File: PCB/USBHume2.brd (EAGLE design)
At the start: 45.1 x 29.8 mm, 23 parts, among them IC1 LM1117MP-3.3

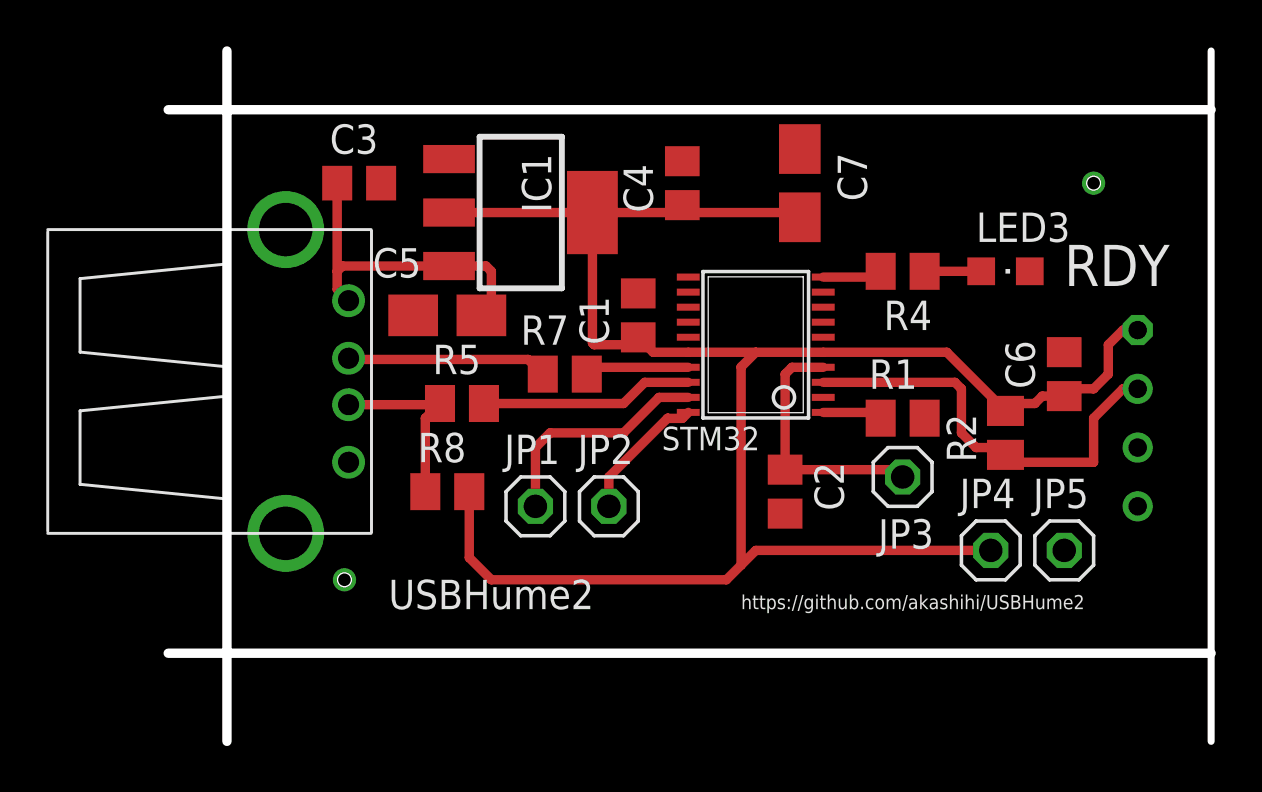
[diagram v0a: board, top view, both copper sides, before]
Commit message: Parts sizes fixed. Board errors fixed.
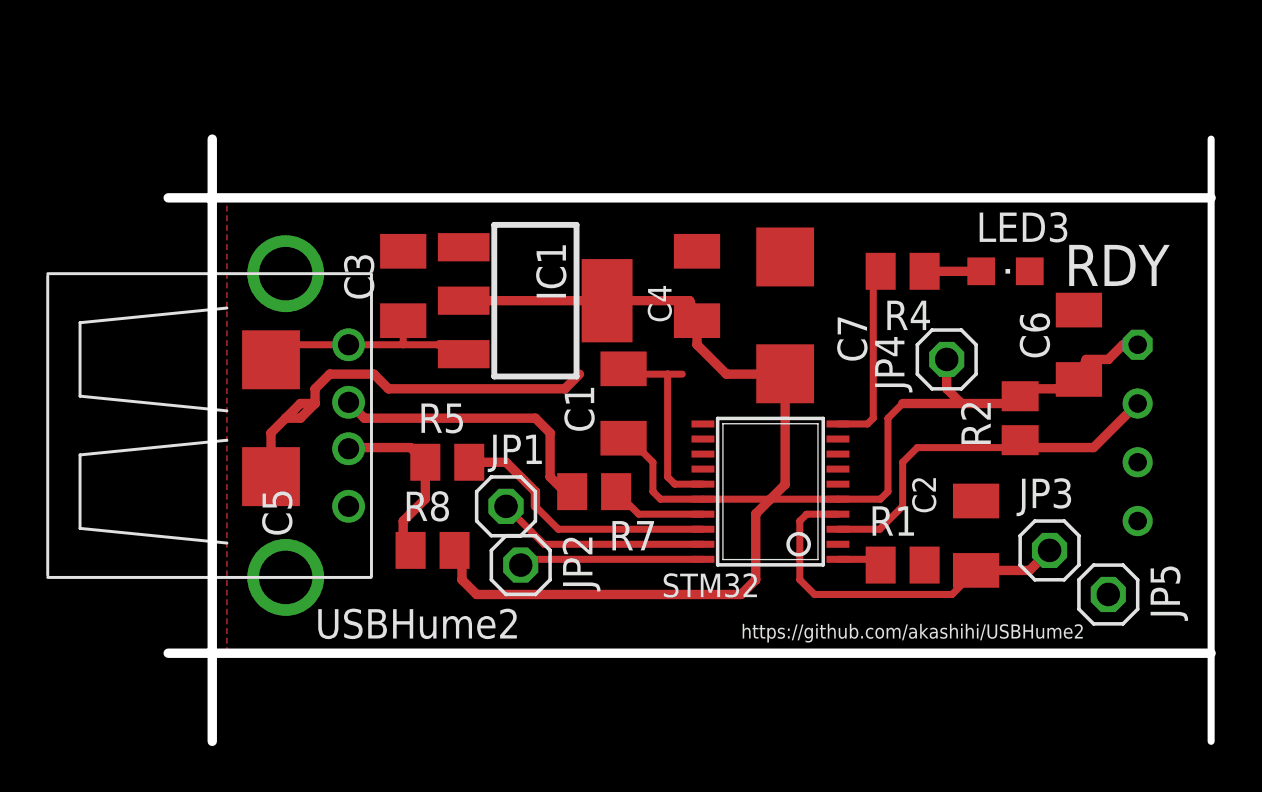
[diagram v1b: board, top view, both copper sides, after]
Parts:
- C1, C2, C3, C4, C6: device rcl:C0805 -> rcl:C1206K
- C5, C7: device rcl:A/3216-18W -> rcl:C/6032-28R
- moved C5 8.82 mm to (4.45, 14.0), turned to 90 degrees
- moved JP4 8.47 mm to (33.7, 16.5), turned to 90 degrees
- moved C2 8.47 mm to (34.9, 8.89), turned to 90 degrees
- moved JP3 7.10 mm to (38.1, 8.26), turned to 0 degrees
- moved STM32 6.38 mm to (26.0, 10.8)
- moved R1 6.35 mm to (31.8, 7.62)
- moved C7 5.75 mm to (26.7, 18.4)
- moved R7 5.24 mm to (18.4, 10.8)
- moved C3 4.84 mm to (10.2, 19.7), turned to 90 degrees
- moved JP2 4.58 mm to (15.2, 7.62), turned to 270 degrees
- moved C4 4.49 mm to (22.9, 19.7)
- moved C1 3.86 mm to (19.7, 14.6)
- moved IC1 3.86 mm to (15.9, 19.1)
- moved JP5 2.69 mm to (40.6, 6.35), turned to 270 degrees
- moved R5 2.62 mm to (12.1, 12.1)
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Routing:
- net GND: track 0.00 -> 27.4 mm
- net +3V3: track 84.2 -> 71.3 mm
- net N$2: track 2.73 -> 8.87 mm
- net N$15: track 11.1 -> 16.2 mm
- net +5V: track 14.2 -> 9.72 mm
- net N$16: track 8.68 -> 12.8 mm
- net N$5: track 9.21 -> 11.7 mm
- net N$10: track 5.86 -> 7.98 mm
- net N$1: track 18.6 -> 17.0 mm
- net N$9: track 10.0 -> 9.19 mm
- net N$7: track 2.59 -> 1.95 mm
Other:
- board size 45.1 x 29.8 mm -> 45.1 x 26 mm

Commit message: Board simplification
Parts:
- removed JP3: NRST, pinhead:1X01
- removed R5, R7: 33, rcl:M0805
- removed R8: 1k5, rcl:M0805
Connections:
- removed net N$16: R7.1, X1.D-
- removed net N$17: R5.1, R8.1, X1.D+
- net +3V3: no longer R8.2
- net N$15: no longer JP3.1
- net N$3: now also X1.D-; no longer R7.2
- net N$5: now also X1.D+; no longer R5.2
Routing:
- net +3V3: track 71.3 -> 53.0 mm
- net N$3: track 4.16 -> 18.8 mm
- net N$16: track 12.8 -> 0.00 mm
- net N$17: track 7.94 -> 0.00 mm
- net N$5: track 11.7 -> 17.9 mm
- net N$15: track 16.2 -> 12.6 mm
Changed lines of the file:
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@@
 </class>
 </classes>
-<designrules name="default *">
+<designrules name="elekon">
 <description language="de">&lt;b&gt;EAGLE Design Rules&lt;/b&gt;
 &lt;p&gt;
@@
 <attribute name="VALUE" x="37.025" y="7.29" size="1.016" layer="27" rot="R90"/>
 </element>
-<element name="JP3" library="pinhead" package="1X01" value="NRST" x="38.1" y="8.255"/>
 <element name="JP4" library="pinhead" package="1X01" value="3V3" x="33.655" y="16.51" rot="R90"/>
 <element name="JP5" library="pinhead" package="1X01" value="GND" x="40.64" y="6.35" rot="R270"/>
@@
 <attribute name="VALUE" x="24.345" y="20.365" size="1.27" layer="27" rot="R270"/>
 </element>
-<element name="R5" library="rcl" package="M0805" value="33" x="12.065" y="12.065"/>
-<element name="R7" library="rcl" package="M0805" value="33" x="18.415" y="10.795" smashed="yes">
-<attribute name="NAME" x="19.05" y="8.255" size="1.27" layer="25"/>
-<attribute name="VALUE" x="17.145" y="8.255" size="1.27" layer="27"/>
-</element>
-<element name="R8" library="rcl" package="M0805" value="1k5" x="11.43" y="8.255"/>
 </elements>
 <signals>
@@
 <signal name="N$3">
 <contactref element="STM32" pad="17"/>
-<contactref element="R7" pad="2"/>
-<wire x1="23.1172" y1="9.82" x2="20.34" y2="9.82" width="0.3048" layer="1"/>
-<wire x1="20.34" y1="9.82" x2="19.365" y2="10.795" width="0.3048" layer="1"/>
+<contactref element="X1" pad="D-"/>
+<wire x1="23.1172" y1="9.82" x2="18.755" y2="9.82" width="0.3048" layer="1"/>
+<wire x1="18.755" y1="9.82" x2="17.78" y2="10.795" width="0.3048" layer="1"/>
+<wire x1="17.78" y1="10.795" x2="17.78" y2="13.335" width="0.3048" layer="1"/>
+<wire x1="17.78" y1="13.335" x2="17.145" y2="13.97" width="0.3048" layer="1"/>
+<wire x1="17.145" y1="13.97" x2="8.4836" y2="13.97" width="0.3048" layer="1"/>
+<wire x1="8.4836" y1="13.97" x2="7.7978" y2="14.6558" width="0.3048" layer="1"/>
 </signal>
 <signal name="N$5">
 <contactref element="STM32" pad="18"/>
-<contactref element="R5" pad="2"/>
-<wire x1="23.1172" y1="9.17" x2="16.865" y2="9.17" width="0.3048" layer="1"/>
-<wire x1="16.865" y1="9.17" x2="15.875" y2="10.16" width="0.3048" layer="1"/>
-<wire x1="15.875" y1="10.16" x2="15.875" y2="10.795" width="0.4064" layer="1"/>
-<wire x1="15.875" y1="10.795" x2="14.605" y2="12.065" width="0.4064" layer="1"/>
-<wire x1="14.605" y1="12.065" x2="13.015" y2="12.065" width="0.4064" layer="1"/>
+<contactref element="X1" pad="D+"/>
+<wire x1="23.1172" y1="9.17" x2="18.135" y2="9.17" width="0.3048" layer="1"/>
+<wire x1="18.135" y1="9.17" x2="17.145" y2="10.16" width="0.3048" layer="1"/>
+<wire x1="17.145" y1="10.16" x2="17.145" y2="12.065" width="0.3048" layer="1"/>
+<wire x1="17.145" y1="12.065" x2="16.51" y2="12.7" width="0.3048" layer="1"/>
+<wire x1="16.51" y1="12.7" x2="7.8486" y2="12.7" width="0.3048" layer="1"/>
+<wire x1="7.8486" y1="12.7" x2="7.7978" y2="12.6492" width="0.3048" layer="1"/>
 </signal>
 <signal name="+3V3">
@@
 <contactref element="C4" pad="1"/>
 <contactref element="C7" pad="+"/>
-<contactref element="R8" pad="2"/>
 <wire x1="12.7762" y1="19.05" x2="18.974" y2="19.05" width="0.4064" layer="1"/>
 <wire x1="18.974" y1="19.05" x2="22.545" y2="19.05" width="0.4064" layer="1"/>
@@
 <wire x1="20.32" y1="12.7" x2="20.09" y2="12.7" width="0.3048" layer="1"/>
 <wire x1="20.09" y1="12.7" x2="19.685" y2="13.105" width="0.3048" layer="1"/>
-<wire x1="25.4" y1="9.835" x2="26.035" y2="10.47" width="0.4064" layer="1"/>
-<wire x1="26.035" y1="10.47" x2="26.67" y2="11.105" width="0.4064" layer="1"/>
-<wire x1="25.4" y1="9.835" x2="25.4" y2="6.985" width="0.4064" layer="1"/>
-<wire x1="25.4" y1="6.985" x2="24.765" y2="6.35" width="0.4064" layer="1"/>
-<wire x1="24.765" y1="6.35" x2="13.335" y2="6.35" width="0.4064" layer="1"/>
-<wire x1="13.335" y1="6.35" x2="12.7" y2="6.985" width="0.4064" layer="1"/>
-<wire x1="12.7" y1="6.985" x2="12.7" y2="7.935" width="0.4064" layer="1"/>
-<wire x1="12.7" y1="7.935" x2="12.38" y2="8.255" width="0.4064" layer="1"/>
 <wire x1="28.9528" y1="10.47" x2="26.035" y2="10.47" width="0.3048" layer="1"/>
 <wire x1="26.035" y1="10.47" x2="23.1172" y2="10.47" width="0.3048" layer="1"/>
+<wire x1="26.67" y1="11.105" x2="26.035" y2="10.47" width="0.3048" layer="1"/>
 </signal>
 <signal name="N$7">
@@
 <contactref element="STM32" pad="4"/>
 <contactref element="C2" pad="1"/>
-<contactref element="JP3" pad="1"/>
 <wire x1="28.9528" y1="9.82" x2="27.6" y2="9.82" width="0.3048" layer="1"/>
 <wire x1="27.6" y1="9.82" x2="27.305" y2="9.525" width="0.3048" layer="1"/>
@@
 <wire x1="27.94" y1="6.35" x2="33.885" y2="6.35" width="0.3048" layer="1"/>
 <wire x1="33.885" y1="6.35" x2="34.925" y2="7.39" width="0.3048" layer="1"/>
-<wire x1="34.925" y1="7.39" x2="37.235" y2="7.39" width="0.4064" layer="1"/>
-<wire x1="37.235" y1="7.39" x2="38.1" y2="8.255" width="0.4064" layer="1"/>
-</signal>
-<signal name="N$16">
-<contactref element="X1" pad="D-"/>
-<contactref element="R7" pad="1"/>
-<wire x1="7.8486" y1="14.605" x2="7.7978" y2="14.6558" width="0.4064" layer="1"/>
-<wire x1="15.875" y1="13.97" x2="8.4836" y2="13.97" width="0.4064" layer="1"/>
-<wire x1="8.4836" y1="13.97" x2="7.7978" y2="14.6558" width="0.4064" layer="1"/>
-<wire x1="16.51" y1="13.335" x2="15.875" y2="13.97" width="0.4064" layer="1"/>
-<wire x1="17.465" y1="10.795" x2="17.78" y2="10.795" width="0.4064" layer="1"/>
-<wire x1="17.465" y1="10.795" x2="17.145" y2="10.795" width="0.4064" layer="1"/>
-<wire x1="17.145" y1="10.795" x2="16.51" y2="11.43" width="0.4064" layer="1"/>
-<wire x1="16.51" y1="11.43" x2="16.51" y2="13.335" width="0.4064" layer="1"/>
-</signal>
-<signal name="N$17">
-<contactref element="R5" pad="1"/>
-<contactref element="X1" pad="D+"/>
-<contactref element="R8" pad="1"/>
-<wire x1="10.48" y1="12.7" x2="7.8486" y2="12.7" width="0.4064" layer="1"/>
-<wire x1="7.8486" y1="12.7" x2="7.7978" y2="12.6492" width="0.4064" layer="1"/>
-<wire x1="10.48" y1="12.7" x2="11.115" y2="12.065" width="0.4064" layer="1"/>
-<wire x1="11.115" y1="12.065" x2="11.115" y2="10.48" width="0.4064" layer="1"/>
-<wire x1="11.115" y1="10.48" x2="10.16" y2="9.525" width="0.4064" layer="1"/>
-<wire x1="10.16" y1="9.525" x2="10.16" y2="8.575" width="0.4064" layer="1"/>
-<wire x1="10.16" y1="8.575" x2="10.48" y2="8.255" width="0.4064" layer="1"/>
 </signal>
 <signal name="N$2">

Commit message: Programming pins grouped
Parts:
- removed JP2: SWDCLK, pinhead:1X01
- removed JP4: 3V3, pinhead:1X01
- removed JP5: GND, pinhead:1X01
- added JP3: (no value), pinhead:1X02
- JP1: value SWDIO -> (none); device pinhead:1X01 -> pinhead:1X02
- moved JP1 20.3 mm to (33.7, 17.1)
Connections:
- net +3V3: now also JP1.1; no longer JP4.1
- net GND: now also JP1.2; no longer JP5.1
- net N$10: now also JP3.2; no longer JP2.1
- net N$9: now also JP3.1; no longer JP1.1
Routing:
- net +3V3: track 53.0 -> 53.6 mm
- net N$10: track 7.98 -> 8.55 mm
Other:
- board text added: "SWDCLK"
- board text added: "SWDIO"
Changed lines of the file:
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@@
 <wire x1="1.905" y1="3.81" x2="0" y2="3.81" width="0.4064" layer="20"/>
 <wire x1="45.085" y1="26.035" x2="45.085" y2="23.495" width="0.3048" layer="20"/>
-<text x="6.35" y="4.445" size="1.27" layer="25">USBHume2</text>
+<text x="7.62" y="5.08" size="1.27" layer="25">USBHume2</text>
 <text x="38.735" y="19.685" size="1.778" layer="25">RDY</text>
-<text x="24.765" y="4.445" size="0.6096" layer="25">https://github.com/akashihi/USBHume2</text>
+<text x="24.13" y="5.08" size="0.6096" layer="25">https://github.com/akashihi/USBHume2</text>
 <wire x1="45.085" y1="23.495" x2="45.085" y2="0" width="0.3048" layer="20"/>
+<text x="9.525" y="9.525" size="0.6096" layer="25">SWDIO</text>
+<text x="9.525" y="7.62" size="0.6096" layer="25">SWDCLK</text>
 </plain>
 <attributes>
@@
 <attribute name="VALUE" x="33.02" y="10.16" size="1.27" layer="27" rot="R180"/>
 </element>
-<element name="JP1" library="pinhead" package="1X01" value="SWDIO" x="14.605" y="10.16" smashed="yes">
-<attribute name="NAME" x="13.8938" y="11.9888" size="1.27" layer="25" ratio="10"/>
-<attribute name="VALUE" x="13.335" y="6.985" size="1.27" layer="27"/>
-</element>
-<element name="JP2" library="pinhead" package="1X01" value="SWDCLK" x="15.24" y="7.62" rot="R270"/>
-<element name="R4" library="rcl" package="M0805" value="1k" x="31.75" y="20.32" rot="R180"/>
+<element name="R4" library="rcl" package="M0805" value="1k" x="31.75" y="20.32" smashed="yes" rot="R180">
+<attribute name="NAME" x="33.02" y="22.86" size="1.27" layer="25" rot="R180"/>
+<attribute name="VALUE" x="33.02" y="22.86" size="1.27" layer="27" rot="R180"/>
+</element>
 <element name="LED3" library="led" package="CHIPLED_0805" value="ACT" x="36.195" y="20.32" rot="R270"/>
 <element name="C2" library="rcl" package="C1206K" value="100n" x="34.925" y="8.89" smashed="yes" rot="R90">
@@
 <attribute name="VALUE" x="37.025" y="7.29" size="1.016" layer="27" rot="R90"/>
 </element>
-<element name="JP4" library="pinhead" package="1X01" value="3V3" x="33.655" y="16.51" rot="R90"/>
-<element name="JP5" library="pinhead" package="1X01" value="GND" x="40.64" y="6.35" rot="R270"/>
 <element name="IC1" library="lm1117mp" package="SOT223" value="LM1117MP-3.3" x="15.875" y="19.05" rot="R270"/>
 <element name="C3" library="rcl" package="C1206K" value="100n" x="10.16" y="19.685" smashed="yes" rot="R90">
@@
 <attribute name="NAME" x="28.94" y="18.46" size="1.27" layer="25" rot="R270"/>
 <attribute name="VALUE" x="24.345" y="20.365" size="1.27" layer="27" rot="R270"/>
+</element>
+<element name="JP3" library="pinhead" package="1X02" value="" x="14.605" y="8.89" rot="R270"/>
+<element name="JP1" library="pinhead" package="1X02" value="" x="33.655" y="17.145" smashed="yes">
+<attribute name="NAME" x="31.0388" y="13.8938" size="1.27" layer="25" ratio="10"/>
+<attribute name="VALUE" x="31.115" y="13.97" size="1.27" layer="27"/>
 </element>
 </elements>
@@
 <contactref element="C6" pad="2"/>
 <polygon width="0.4064" layer="1" isolate="0.6096">
-<vertex x="2.54" y="23.495"/>
+<vertex x="1.905" y="23.495"/>
 <vertex x="45.085" y="23.495"/>
 <vertex x="45.085" y="3.81"/>
-<vertex x="2.54" y="3.81"/>
+<vertex x="1.905" y="3.81"/>
 </polygon>
 <contactref element="STM32" pad="15"/>
@@
 <contactref element="LED3" pad="C"/>
 <contactref element="C2" pad="2"/>
-<contactref element="JP5" pad="1"/>
 <contactref element="IC1" pad="1"/>
 <contactref element="C3" pad="2"/>
@@
 <wire x1="21.9" y1="11.12" x2="21.59" y2="11.43" width="0.3048" layer="1"/>
 <wire x1="21.59" y1="11.43" x2="21.59" y2="15.875" width="0.3048" layer="1"/>
+<contactref element="JP1" pad="2"/>
 </signal>
 <signal name="N$1">
@@
 <contactref element="C6" pad="1"/>
 <contactref element="R2" pad="2"/>
-<contactref element="JP4" pad="1"/>
 <contactref element="IC1" pad="2"/>
 <contactref element="IC1" pad="4"/>
@@
 <wire x1="41.91" y1="17.145" x2="41.275" y2="17.145" width="0.4064" layer="1"/>
 <wire x1="36.83" y1="14.92" x2="36.83" y2="15.24" width="0.4064" layer="1"/>
-<wire x1="31.75" y1="14.605" x2="34.29" y2="14.605" width="0.4064" layer="1"/>
+<wire x1="31.75" y1="14.605" x2="36.515" y2="14.605" width="0.4064" layer="1"/>
 <wire x1="36.515" y1="14.605" x2="36.83" y2="14.92" width="0.4064" layer="1"/>
-<wire x1="36.515" y1="14.605" x2="34.29" y2="14.605" width="0.4064" layer="1"/>
-<wire x1="34.29" y1="14.605" x2="33.655" y2="15.24" width="0.4064" layer="1"/>
-<wire x1="33.655" y1="15.24" x2="33.655" y2="16.51" width="0.4064" layer="1"/>
 <wire x1="36.83" y1="15.24" x2="38.415" y2="15.24" width="0.4064" layer="1"/>
 <wire x1="38.415" y1="15.24" x2="39.37" y2="15.645" width="0.4064" layer="1"/>
@@
 <wire x1="26.035" y1="10.47" x2="23.1172" y2="10.47" width="0.3048" layer="1"/>
 <wire x1="26.67" y1="11.105" x2="26.035" y2="10.47" width="0.3048" layer="1"/>
+<contactref element="JP1" pad="1"/>
+<wire x1="32.385" y1="17.145" x2="32.385" y2="15.24" width="0.3048" layer="1"/>
+<wire x1="32.385" y1="15.24" x2="31.75" y2="14.605" width="0.3048" layer="1"/>
 </signal>
 <signal name="N$7">
@@
 <signal name="N$9">
 <contactref element="STM32" pad="19"/>
-<contactref element="JP1" pad="1"/>
-<wire x1="23.1172" y1="8.52" x2="16.245" y2="8.52" width="0.3048" layer="1"/>
-<wire x1="16.245" y1="8.52" x2="14.605" y2="10.16" width="0.3048" layer="1"/>
+<contactref element="JP3" pad="1"/>
+<wire x1="23.1172" y1="8.52" x2="17.515" y2="8.52" width="0.3048" layer="1"/>
+<wire x1="17.515" y1="8.52" x2="15.875" y2="10.16" width="0.3048" layer="1"/>
+<wire x1="15.875" y1="10.16" x2="14.605" y2="10.16" width="0.3048" layer="1"/>
 </signal>
 <signal name="N$10">
-<contactref element="JP2" pad="1"/>
 <contactref element="STM32" pad="20"/>
+<contactref element="JP3" pad="2"/>
 <wire x1="23.1172" y1="7.87" x2="15.49" y2="7.87" width="0.3048" layer="1"/>
-<wire x1="15.49" y1="7.87" x2="15.24" y2="7.62" width="0.3048" layer="1"/>
+<wire x1="15.49" y1="7.87" x2="14.605" y2="7.62" width="0.3048" layer="1"/>
 </signal>
 <signal name="N$14">
